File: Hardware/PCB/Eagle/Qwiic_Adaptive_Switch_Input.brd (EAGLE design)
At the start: 43.2 x 43.2 mm, 58 parts, among them J1 QWIIC_RIGHT_ANGLE, J3 QWIIC_RIGHT_ANGLE, SW1 CUI_SJ1-3513, SW2 CUI_SJ1-3513, U1 TCA9534

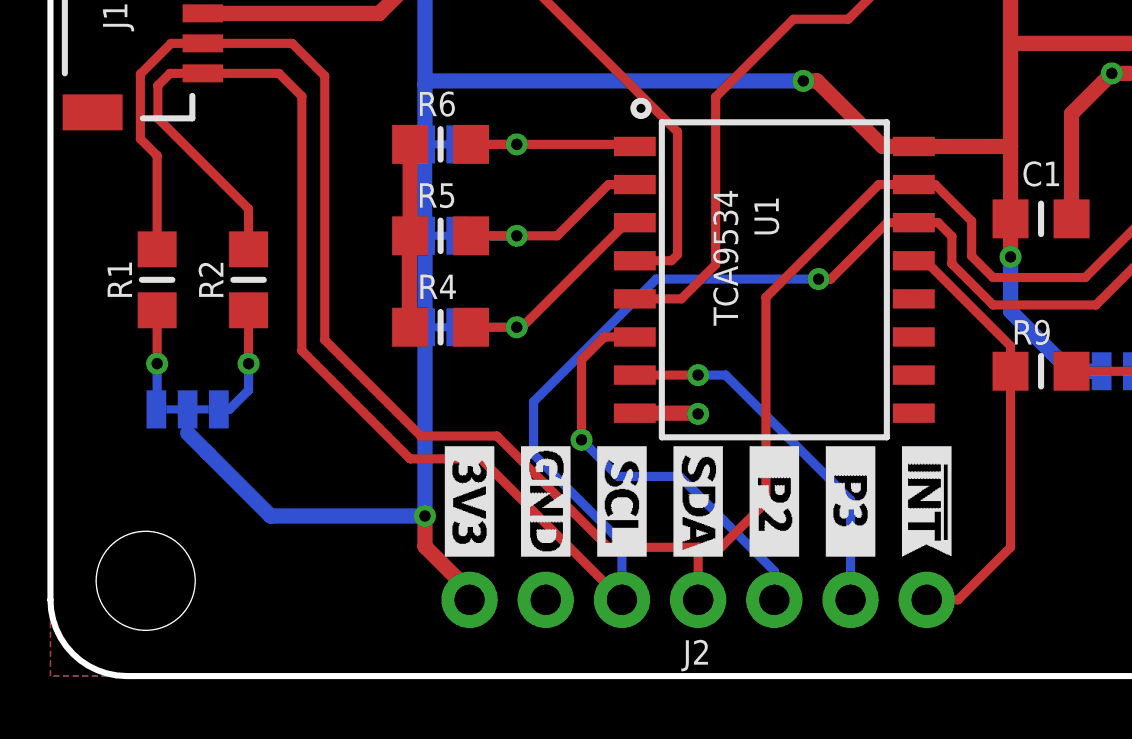
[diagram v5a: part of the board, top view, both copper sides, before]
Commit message: Updated header pin order
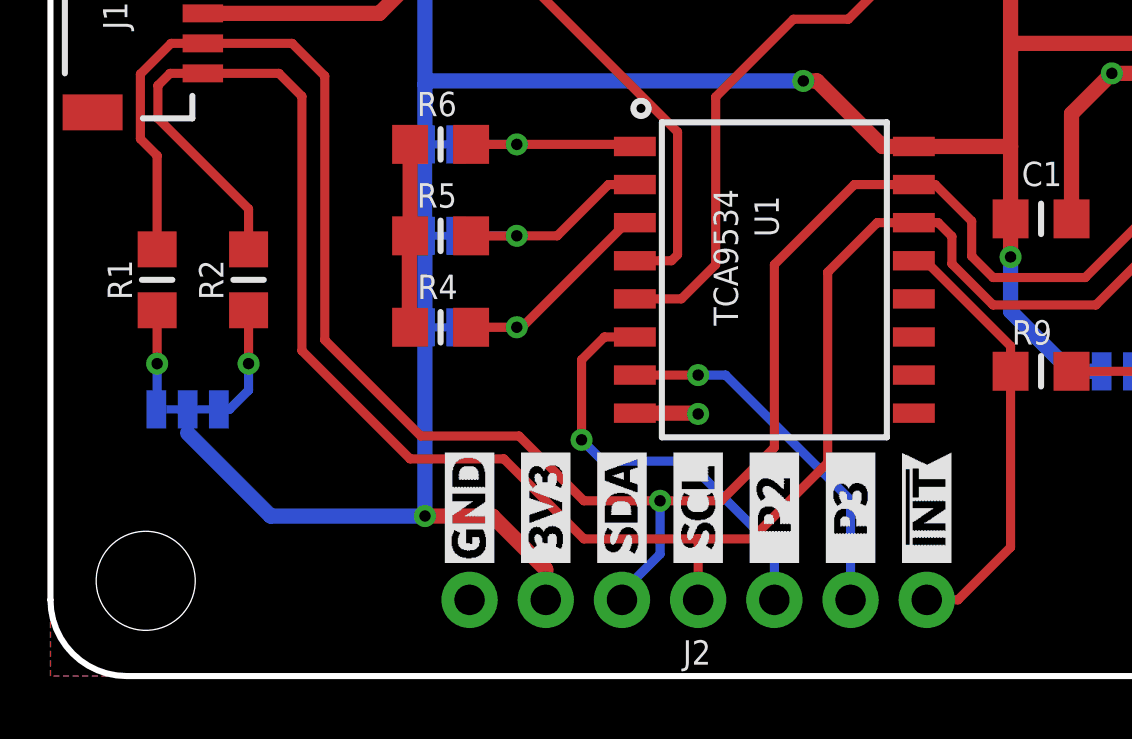
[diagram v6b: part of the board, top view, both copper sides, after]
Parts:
- removed JP3: STAND-OFF-3.3, milador:STAND-OFF-3.3
- added H3: STAND-OFF-3.3, milador:STAND-OFF-3.3
- moved H1 52.1 mm to (3.17, 3.17)
- moved LABEL_3V_TOP 4.58 mm to (16.5, 3.81), turned to 90 degrees
- moved LABEL_GND_TOP 4.58 mm to (14.0, 3.81), turned to 90 degrees
- moved LABE_SCL_TOP 4.58 mm to (21.6, 3.81), turned to 90 degrees
- moved LABE_SDA_TOP 4.58 mm to (19.1, 3.81), turned to 90 degrees
- moved LABEL_!INT_TOP 3.81 mm to (29.2, 3.81), turned to 90 degrees
- moved LABEL_P2_TOP 3.81 mm to (24.1, 3.81), turned to 90 degrees
- moved LABEL_P3_TOP 3.81 mm to (26.7, 3.81), turned to 90 degrees
- moved LABEL_3V_BOTTOM 2.54 mm to (16.5, 3.81)
- moved LABEL_GND_BOTTOM 2.54 mm to (14.0, 3.81)
- moved LABE_SCL_BOTTOM 2.54 mm to (21.6, 3.81)
- moved LABE_SDA_BOTTOM 2.54 mm to (19.1, 3.81)
- renumbered JP4 to H4
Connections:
- net 3.3V: now also J2.2; no longer J2.1
- net GND: now also J2.1; no longer J2.2
- net SCL: now also J2.4; no longer J2.3
- net SDA: now also J2.3; no longer J2.4
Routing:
- net SCL: track 79.6 -> 75.6 mm, vias 1 -> 0
- net 3.3V: track 98.8 -> 101.2 mm
- net SDA: track 74.7 -> 75.0 mm, vias 0 -> 1
